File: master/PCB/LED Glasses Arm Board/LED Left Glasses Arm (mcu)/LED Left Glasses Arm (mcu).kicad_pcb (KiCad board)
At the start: 2 copper layers, 1 part, among them U1 ATmega328P-AU

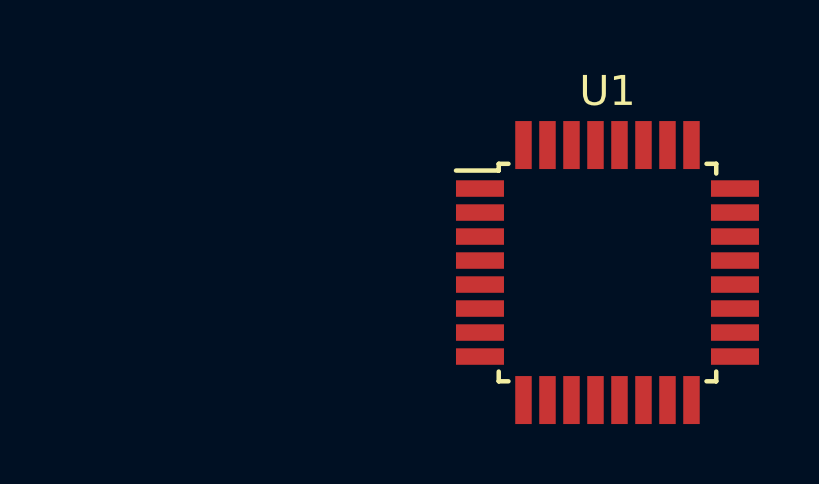
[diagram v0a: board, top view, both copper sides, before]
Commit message: added STM32 board
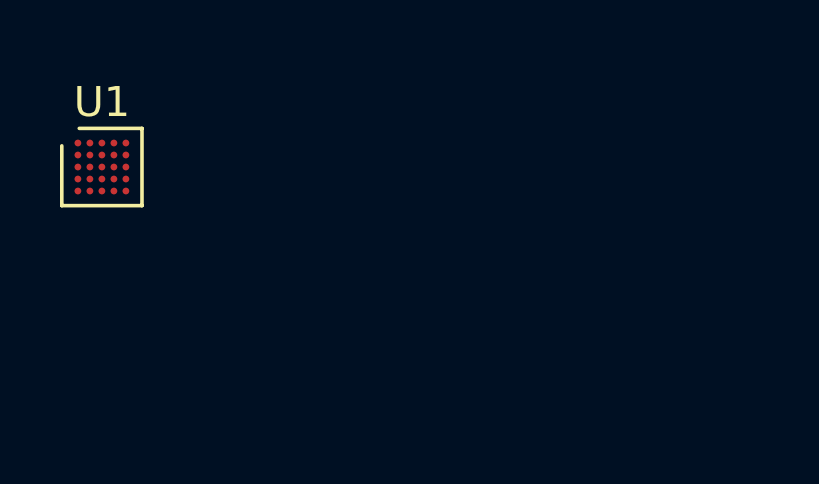
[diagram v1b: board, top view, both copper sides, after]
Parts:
- U1: value ATmega328P-AU -> STM32F031E6Yx; footprint Package_QFP:TQFP-32_7x7mm_P0.8mm -> Package_CSP:ST_WLCSP-25_Die444
- moved U1 17.2 mm to (120.9, 89.2)

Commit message: messing around with the MCU
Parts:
- moved U1 10.4 mm to (130.9, 91.8)
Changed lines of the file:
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@@
   )
   (module Package_CSP:ST_WLCSP-25_Die444 (layer F.Cu)
-    (at 120.8532 89.2048)
+    (at 130.9116 91.8337)
     (descr "WLCSP-25, 5x5 raster, 2.423x2.325mm package, pitch 0.4mm; see section 7.5 of http://www.st.com/resource/en/datasheet/stm32f031k6.pdf")
     (tags "BGA 25 0.4")

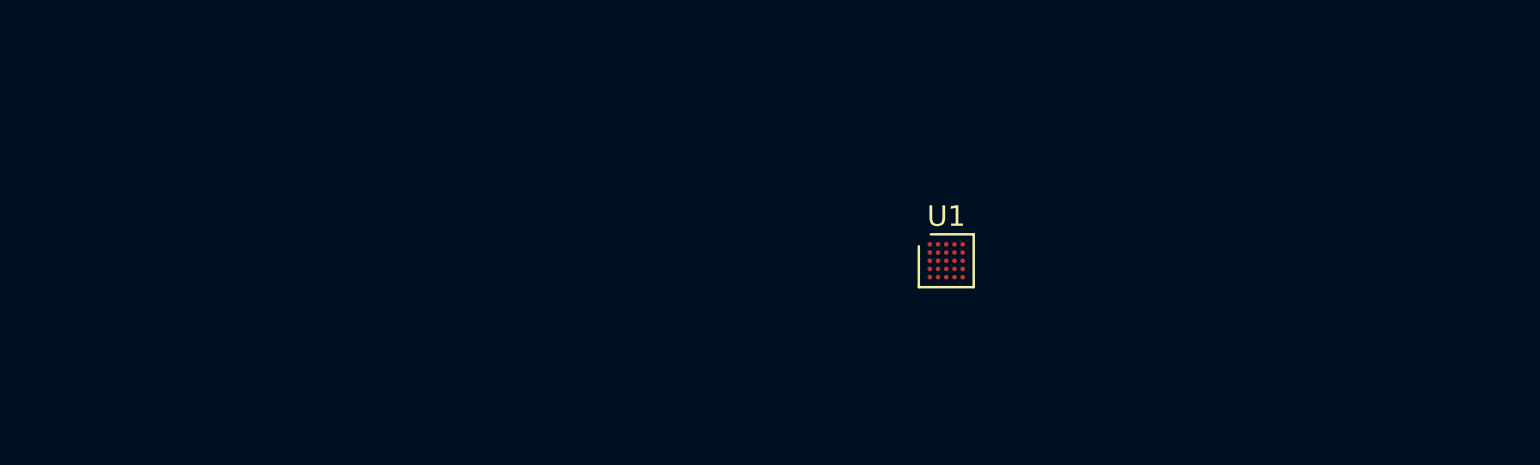
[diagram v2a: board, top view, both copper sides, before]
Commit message: added footprints to the PCB
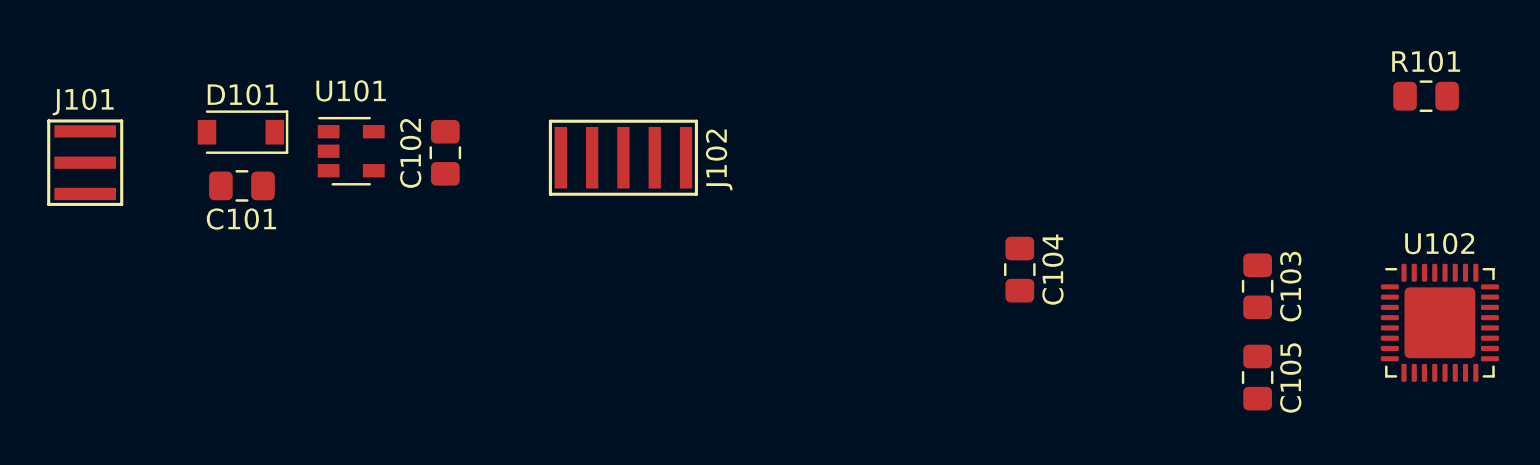
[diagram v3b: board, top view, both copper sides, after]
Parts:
- removed U1: STM32F031E6Yx, Package_CSP:ST_WLCSP-25_Die444
- added C101: 4u7, 25V, Capacitor_SMD:C_0805_2012Metric_Pad1.15x1.40mm_HandSolder, F.Cu at (96.6, 88.2)
- added C102: 4u7, 25V, Capacitor_SMD:C_0805_2012Metric_Pad1.15x1.40mm_HandSolder, F.Cu at (106.5, 86.6)
- added C103: 100n, 25V, Capacitor_SMD:C_0805_2012Metric_Pad1.15x1.40mm_HandSolder, F.Cu at (146.1, 93.1)
- added C104: 100n, 25V, Capacitor_SMD:C_0805_2012Metric_Pad1.15x1.40mm_HandSolder, F.Cu at (134.5, 92.3)
- added C105: 100n, 25V, Capacitor_SMD:C_0805_2012Metric_Pad1.15x1.40mm_HandSolder, F.Cu at (146.1, 97.5)
- added D101: MBR0520LT1G, Diode_SMD:D_SOD-123, F.Cu at (96.6, 85.6)
- added J101: Front Connector, Connector_PinHeader_1.00mm:PinHeader_1x03_P1.00mm_Vertical_SMD_Pin1Left_CUSTOM, F.Cu at (89.0, 87.6)
- added J102: SWD, Connector_PinHeader_1.00mm:PinHeader_1x05_P1.00mm_Vertical_SMD_Pin1Left_CUSTOM, F.Cu at (116.2, 86.8)
- added R101: 100k, 1/16W, Resistor_SMD:R_0805_2012Metric_Pad1.15x1.40mm_HandSolder, F.Cu at (154.3, 83.8)
- added U101: MIC5504-3.3YM5, Package_TO_SOT_SMD:SOT-23-5, F.Cu at (101.9, 86.5)
- added U102: STM32G071KBU6, Package_DFN_QFN:QFN-32-1EP_5x5mm_P0.5mm_EP3.45x3.45mm, F.Cu at (155.0, 94.9)

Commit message: footprints in misc-footprints library
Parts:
- added MK101: SPH0641LM4H-1, misc-footprints:MIC_SPH0641LM4H-1, F.Cu at (114.5, 87.4)
- J101: footprint Connector_PinHeader_1.00mm:PinHeader_1x03_P1.00mm_Vertical_SMD_Pin1Left_CUSTOM -> misc-footprints:PinHeader_1x03_P1.00mm_Vertical_SMD_Pin1Left_CUSTOM
- J102: footprint Connector_PinHeader_1.00mm:PinHeader_1x05_P1.00mm_Vertical_SMD_Pin1Left_CUSTOM -> misc-footprints:PinHeader_1x05_P1.00mm_Vertical_SMD_Pin1Left_CUSTOM
- U102: footprint Package_DFN_QFN:QFN-32-1EP_5x5mm_P0.5mm_EP3.45x3.45mm -> misc-footprints:QFN50P500X500X60-33N-D
- moved C104 24.5 mm to (110.4, 87.4)
- moved J102 14.6 mm to (130.2, 91.2)
- moved R101 6.71 mm to (155.0, 90.5), turned to 180 degrees

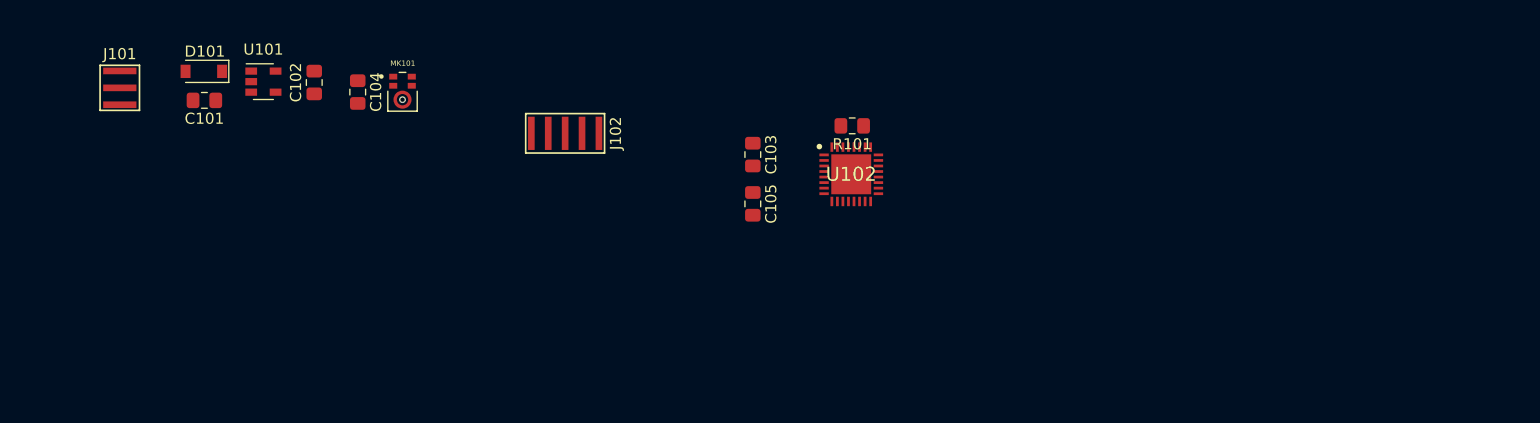
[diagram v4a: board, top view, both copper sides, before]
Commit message: moved outline to edge cuts layer and removed extra lines
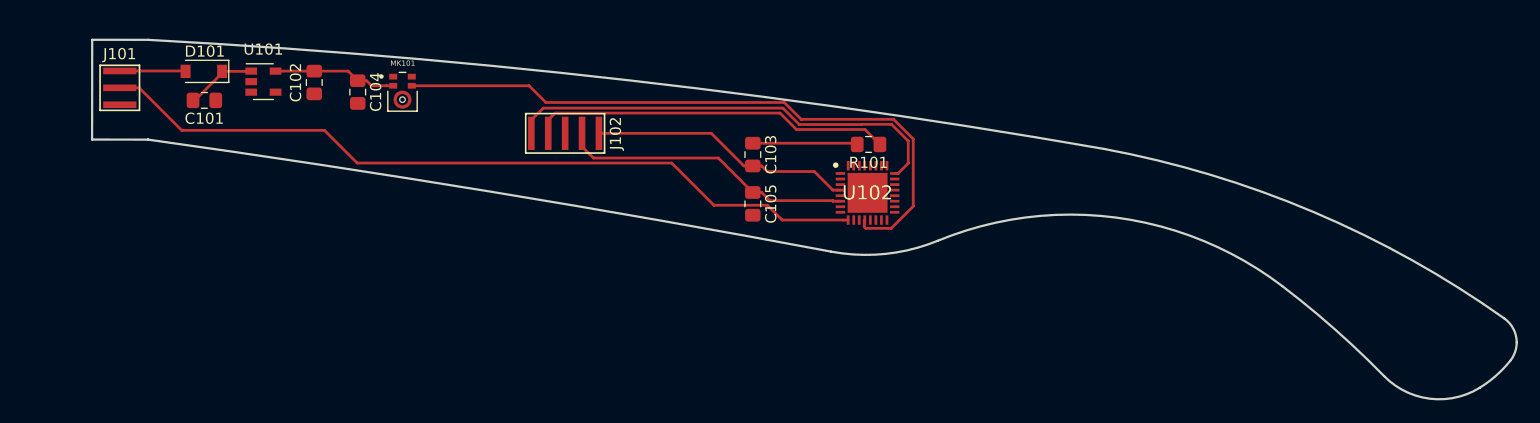
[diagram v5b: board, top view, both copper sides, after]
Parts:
- moved R101 2.23 mm to (156.5, 92.2)
- moved U102 2.23 mm to (156.4, 96.5)
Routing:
- net /LED_DATA: track 0.00 -> 70.6 mm
- net /MIC_CLK: track 0.00 -> 59.3 mm
- net /SWDIO: track 0.00 -> 40.5 mm
- net +3V3: track 0.00 -> 35.1 mm
- net /SWCLK: track 0.00 -> 32.5 mm
- net /NRST: track 0.00 -> 26.6 mm
- net GND: track 0.00 -> 9.46 mm
- net Net-(C101-Pad2): track 0.00 -> 6.43 mm
- net Net-(D101-Pad2): track 0.00 -> 5.95 mm
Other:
- board outline added: 128.5 x 32.4 mm

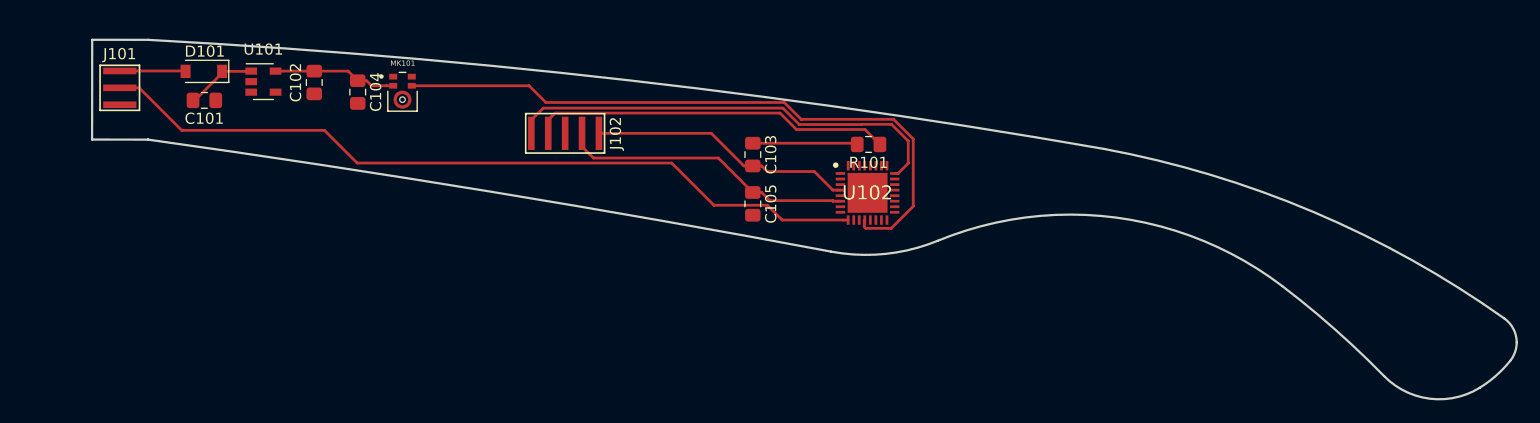
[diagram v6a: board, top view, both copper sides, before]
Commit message: board layout revisions
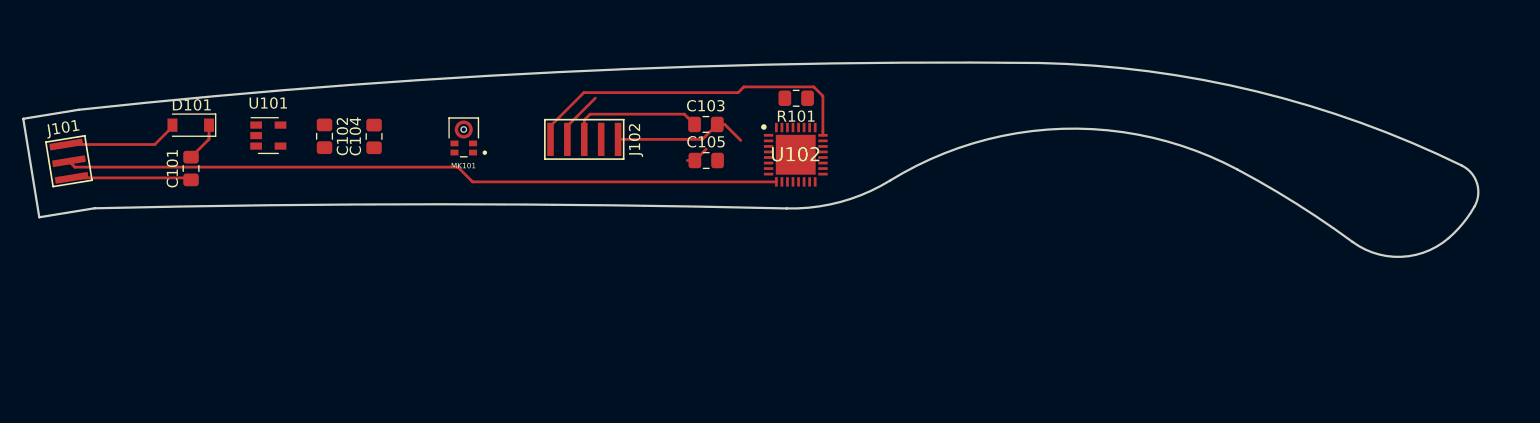
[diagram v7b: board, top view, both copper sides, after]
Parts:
- moved J101 8.00 mm to (84.5, 94.2), turned to 9.25 degrees
- moved R101 7.74 mm to (150.0, 88.0)
- moved U102 7.33 mm to (149.9, 93.1)
- moved MK101 6.89 mm to (120.0, 91.5), turned to 180 degrees
- moved C101 6.26 mm to (95.4, 94.3), turned to 90 degrees
- moved C105 5.74 mm to (141.9, 93.6), turned to 0 degrees
- moved C103 5.03 mm to (141.8, 90.4), turned to 0 degrees
- moved D101 4.99 mm to (95.4, 90.4)
- moved C102 4.94 mm to (107.4, 91.4), turned to 270 degrees
- moved U101 4.88 mm to (102.4, 91.4)
- moved C104 4.26 mm to (111.9, 91.4), turned to 90 degrees
- moved J102 1.81 mm to (131.9, 91.7)
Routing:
- net /MIC_CLK: track 59.3 -> 0.00 mm
- net /SWCLK: track 32.5 -> 4.77 mm
- net /NRST: track 26.6 -> 2.12 mm
- net +3V3: track 35.1 -> 13.4 mm
- net GND: track 9.46 -> 23.4 mm
- net /SWDIO: track 40.5 -> 31.1 mm
- net /LED_DATA: track 70.6 -> 64.6 mm
- net Net-(D101-Pad2): track 5.95 -> 10.4 mm
- net Net-(C101-Pad2): track 6.43 -> 3.56 mm
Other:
- board size 128.5 x 32.4 mm -> 131.2 x 17.5 mm

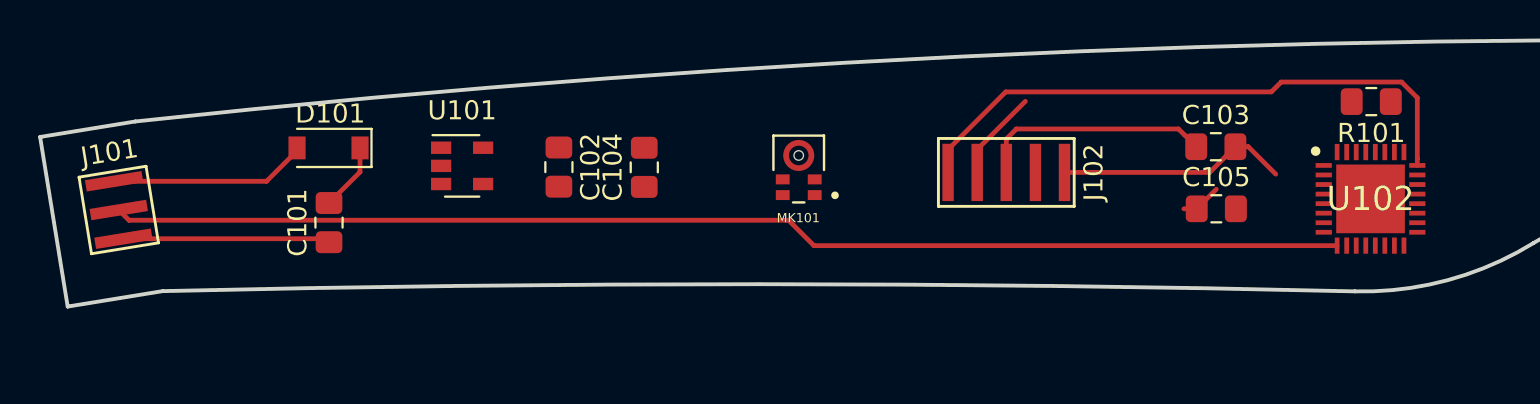
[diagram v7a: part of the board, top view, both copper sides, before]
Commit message: moved components around on mcu arm
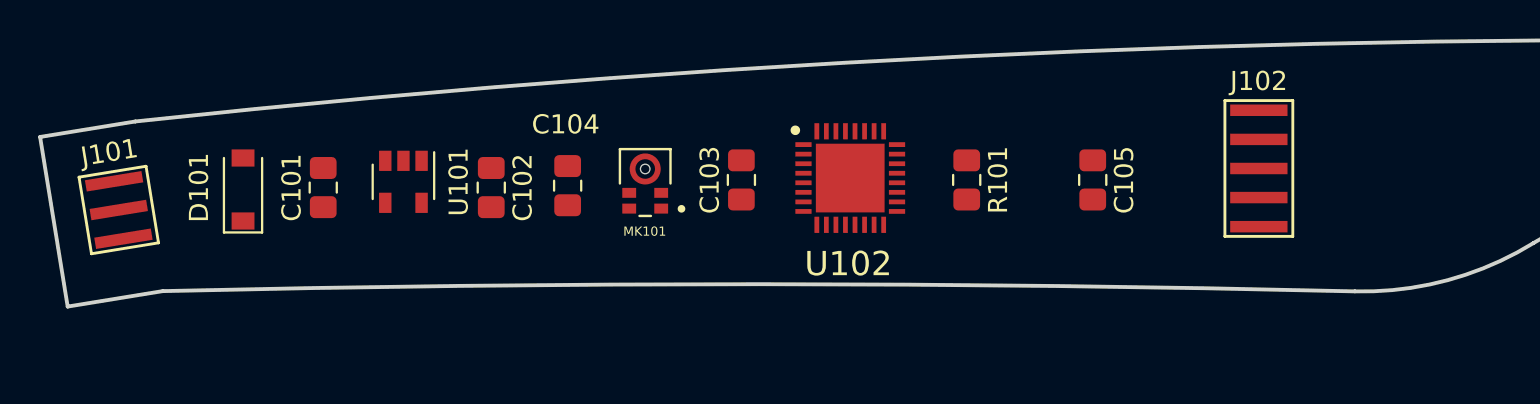
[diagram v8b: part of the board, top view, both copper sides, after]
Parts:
- moved U102 27.3 mm to (122.7, 92.0)
- moved C103 24.9 mm to (117.0, 92.1), turned to 90 degrees
- moved R101 21.6 mm to (128.8, 92.1), turned to 270 degrees
- moved J102 12.3 mm to (144.1, 90.5), turned to 0 degrees
- moved MK101 8.07 mm to (112.0, 92.2)
- moved C105 6.65 mm to (135.4, 92.1), turned to 270 degrees
- moved D101 4.98 mm to (90.9, 92.6), turned to 90 degrees
- moved C104 4.13 mm to (107.9, 92.4)
- moved C102 3.70 mm to (103.9, 92.5)
- moved U101 3.19 mm to (99.3, 92.2), turned to 270 degrees
- moved C101 1.86 mm to (95.1, 92.5)
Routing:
- net /LED_DATA: track 64.6 -> 0.00 mm
- net /SWDIO: track 31.1 -> 0.00 mm
- net GND: track 23.4 -> 0.00 mm
- net +3V3: track 13.4 -> 0.00 mm
- net Net-(D101-Pad2): track 10.4 -> 0.00 mm
- net /SWCLK: track 4.77 -> 0.00 mm
- net Net-(C101-Pad2): track 3.56 -> 0.00 mm
- net /NRST: track 2.12 -> 0.00 mm
